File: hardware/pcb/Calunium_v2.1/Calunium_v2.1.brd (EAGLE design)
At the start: 99.1 x 78.7 mm, 63 parts, among them IC1 MCP1702-3.3, IC2 DS1307, IC3 MCP1702-5.0, IC4 ATMEGA1284, IC5 MCP2200, Q1 2N7000, U1 CALUNIUM-SHIELD, X1 PWR, X2 JTAG, X3 USB, X4 CONN-SMATHD, X5 UART0, X6 MICRO-SD-SOCKETHIROSE-DM3D, Y1 32k768, Y2 16MHz, Y3 12MHz

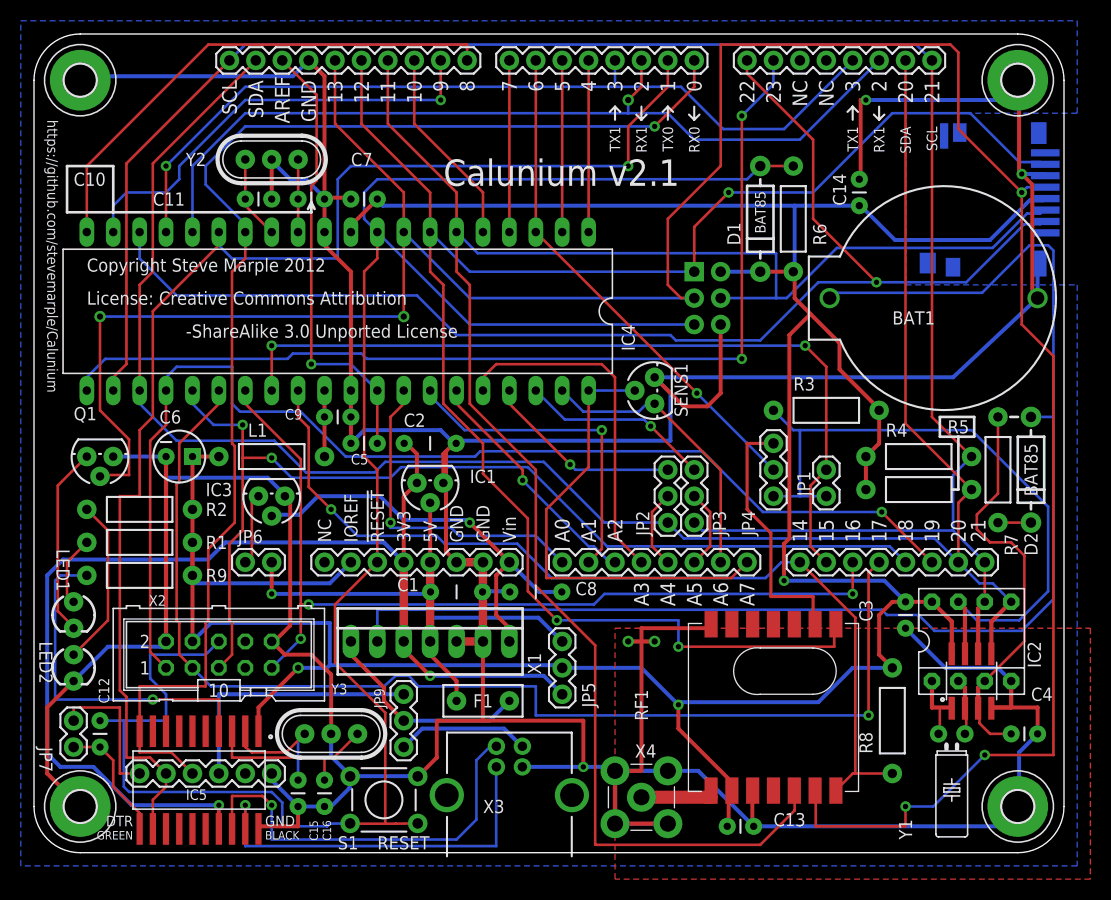
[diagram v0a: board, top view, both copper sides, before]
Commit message: Add load capacitors for MCP7941x RTC. Removed DIP footprint for RTC.
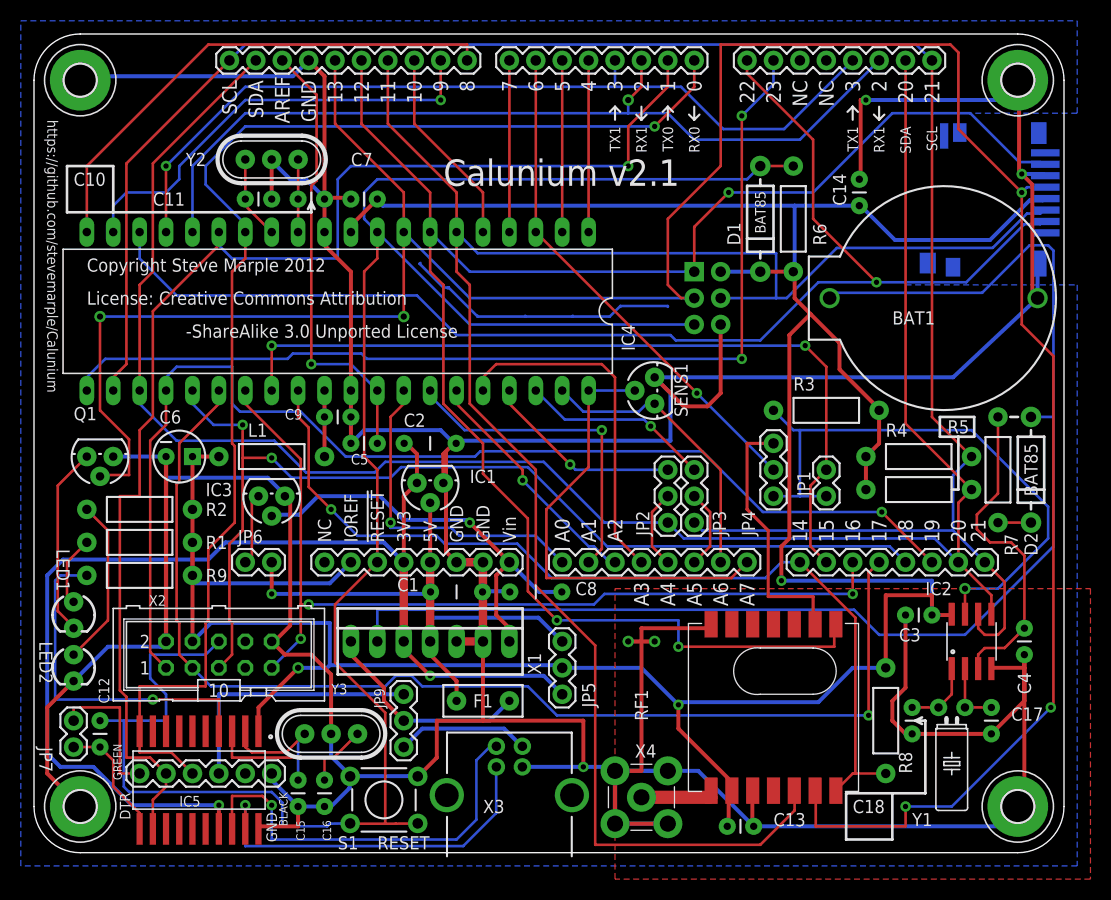
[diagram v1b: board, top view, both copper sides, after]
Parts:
- added C17, C18: 15p, SparkFun:CAP-PTH-SMALL
- IC2: value DS1307 -> DS1338; device SteveMarple:DIL08-SOIC8 -> SteveMarple:SO08
- moved C4 10.2 mm to (95.2, 21.6), turned to 270 degrees
- moved C3 2.84 mm to (86.4, 22.9), turned to 180 degrees
- moved Y1 2.54 mm to (88.3, 14.0)
- moved R8 0.63 mm to (81.9, 12.7)
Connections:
- net 20(SDA): no longer IC2.5@1
- net 21(SCL): no longer IC2.6@1
- net GND: now also C17.2, C18.2; no longer IC2.4@1
- net N$11: no longer IC2.3@1
- net N$12: now also C17.1; no longer IC2.2@1
- net N$5: now also C18.1; no longer IC2.1@1
- net SQW: no longer IC2.7@1
- net VCC: no longer IC2.8@1
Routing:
- net GNDA: track 0.00 -> 27.0 mm
- net GND: track 528.9 -> 549.4 mm
- net VCC: track 302.1 -> 310.6 mm
- net 21(SCL): track 186.3 -> 193.8 mm
- net N$11: track 36.1 -> 31.1 mm
- net SQW: track 60.6 -> 57.2 mm, vias 0 -> 1
- net N$12: track 2.91 -> 6.27 mm
- net 13(SCK): track 262.0 -> 259.3 mm
- net VBATT: track 129.7 -> 127.0 mm
- net N$5: track 4.85 -> 6.80 mm
- net USB_D+: track 38.0 -> 36.1 mm
- net 17(TDO): track 113.5 -> 111.9 mm
- net 14: track 89.8 -> 89.2 mm
- net 20(SDA): track 181.9 -> 181.3 mm
